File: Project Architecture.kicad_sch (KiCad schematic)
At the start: 0 parts

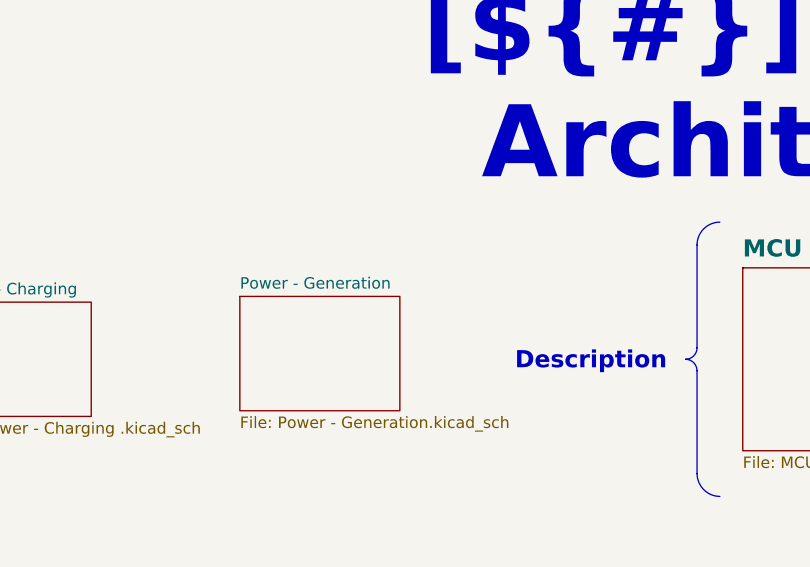
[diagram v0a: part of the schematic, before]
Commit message: added power switch, 5V and 3V3 power generation
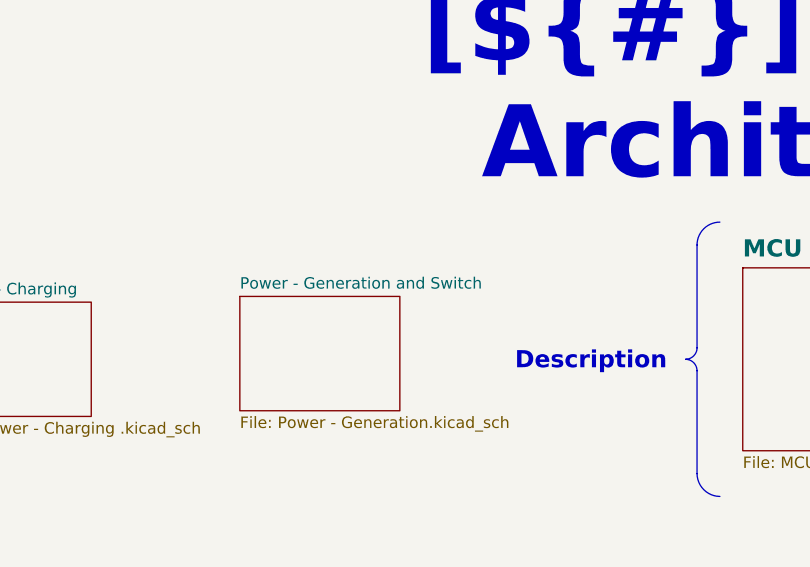
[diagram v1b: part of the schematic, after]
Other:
- sheet Power - Generation renamed Power - Generation and Switch
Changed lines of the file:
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@@
 			(color 0 0 0 0.0000)
 		)
-		(property "Sheetname" "Power - Generation"
+		(property "Sheetname" "Power - Generation and Switch"
 			(at 144.78 49.4534 0)
 			(effects

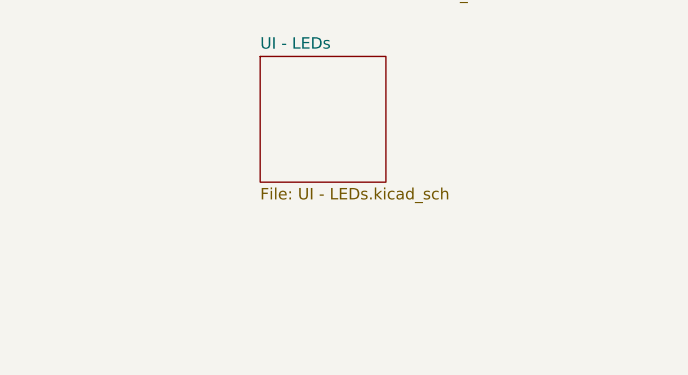
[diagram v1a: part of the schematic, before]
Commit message: added buzzer schematic
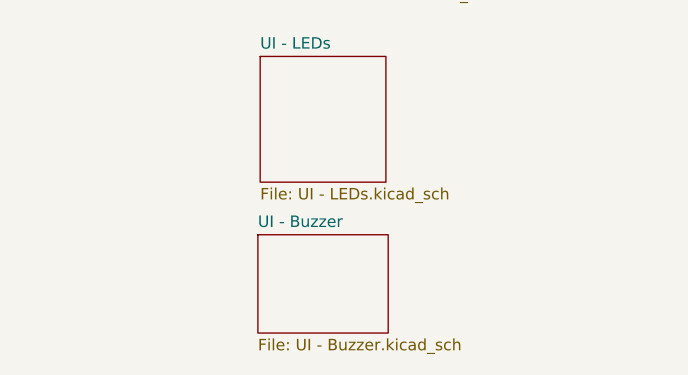
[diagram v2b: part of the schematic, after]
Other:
- added sheet UI - Buzzer (UI - Buzzer.kicad_sch)
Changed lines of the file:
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@@
+	)
+	(sheet
+		(at 282.956 228.092)
+		(size 14.478 10.922)
+		(exclude_from_sim no)
+		(in_bom yes)
+		(on_board yes)
+		(dnp no)
+		(fields_autoplaced yes)
+		(stroke
+			(width 0.1524)
+			(type solid)
+		)
+		(fill
+			(color 0 0 0 0.0000)
+		)
+		(property "Sheetname" "UI - Buzzer"
+			(at 282.956 227.3804 0)
+			(effects
+				(font
+					(size 1.27 1.27)
+				)
+				(justify left bottom)
+			)
+		)
+		(property "Sheetfile" "UI - Buzzer.kicad_sch"
+			(at 282.956 239.5986 0)
+			(effects
+				(font
+					(size 1.27 1.27)
+				)
+				(justify left top)
+			)
+		)
+		(instances
+			(project "transmitter"
+				(path "/0650c7a8-acba-429c-9f8e-eec0baf0bc1c/fede4c36-00cc-4d3d-b71c-5243ba232202"
+					(page "23")
+				)
+			)
+		)
 	)
 	(sheet

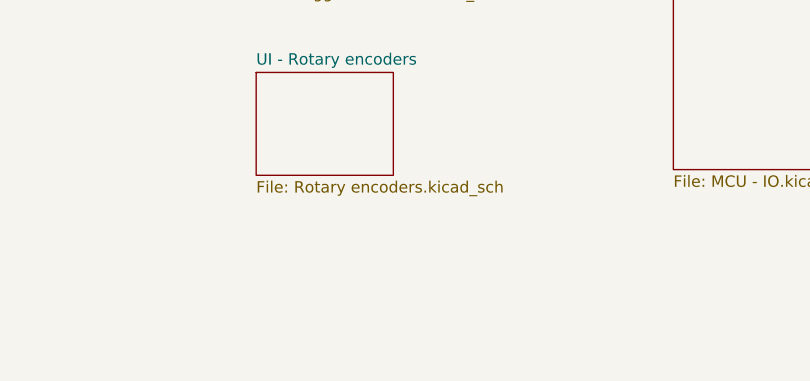
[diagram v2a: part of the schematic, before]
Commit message: added auxiliary schematic, problem with kicad - cannot modify project settings
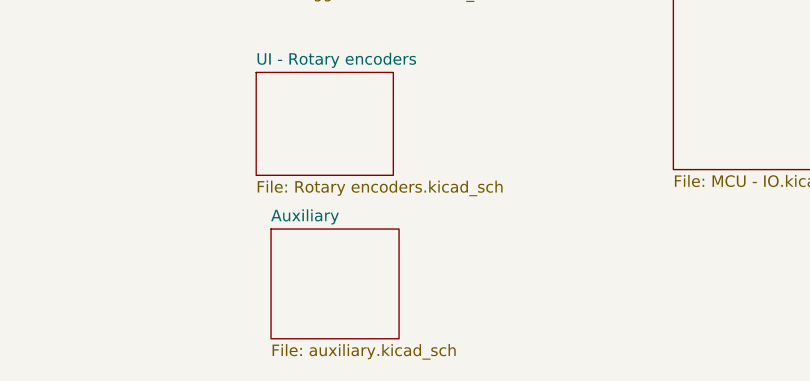
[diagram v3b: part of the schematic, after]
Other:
- added sheet Auxiliary (auxiliary.kicad_sch)
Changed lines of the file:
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@@
+	)
+	(sheet
+		(at 155.956 231.394)
+		(size 14.224 12.192)
+		(exclude_from_sim no)
+		(in_bom yes)
+		(on_board yes)
+		(dnp no)
+		(fields_autoplaced yes)
+		(stroke
+			(width 0.1524)
+			(type solid)
+		)
+		(fill
+			(color 0 0 0 0.0000)
+		)
+		(property "Sheetname" "Auxiliary"
+			(at 155.956 230.6824 0)
+			(effects
+				(font
+					(size 1.27 1.27)
+				)
+				(justify left bottom)
+			)
+		)
+		(property "Sheetfile" "auxiliary.kicad_sch"
+			(at 155.956 244.1706 0)
+			(effects
+				(font
+					(size 1.27 1.27)
+				)
+				(justify left top)
+			)
+		)
+		(instances
+			(project "transmitter"
+				(path "/0650c7a8-acba-429c-9f8e-eec0baf0bc1c/fede4c36-00cc-4d3d-b71c-5243ba232202"
+					(page "24")
+				)
+			)
+		)
 	)
 	(sheet

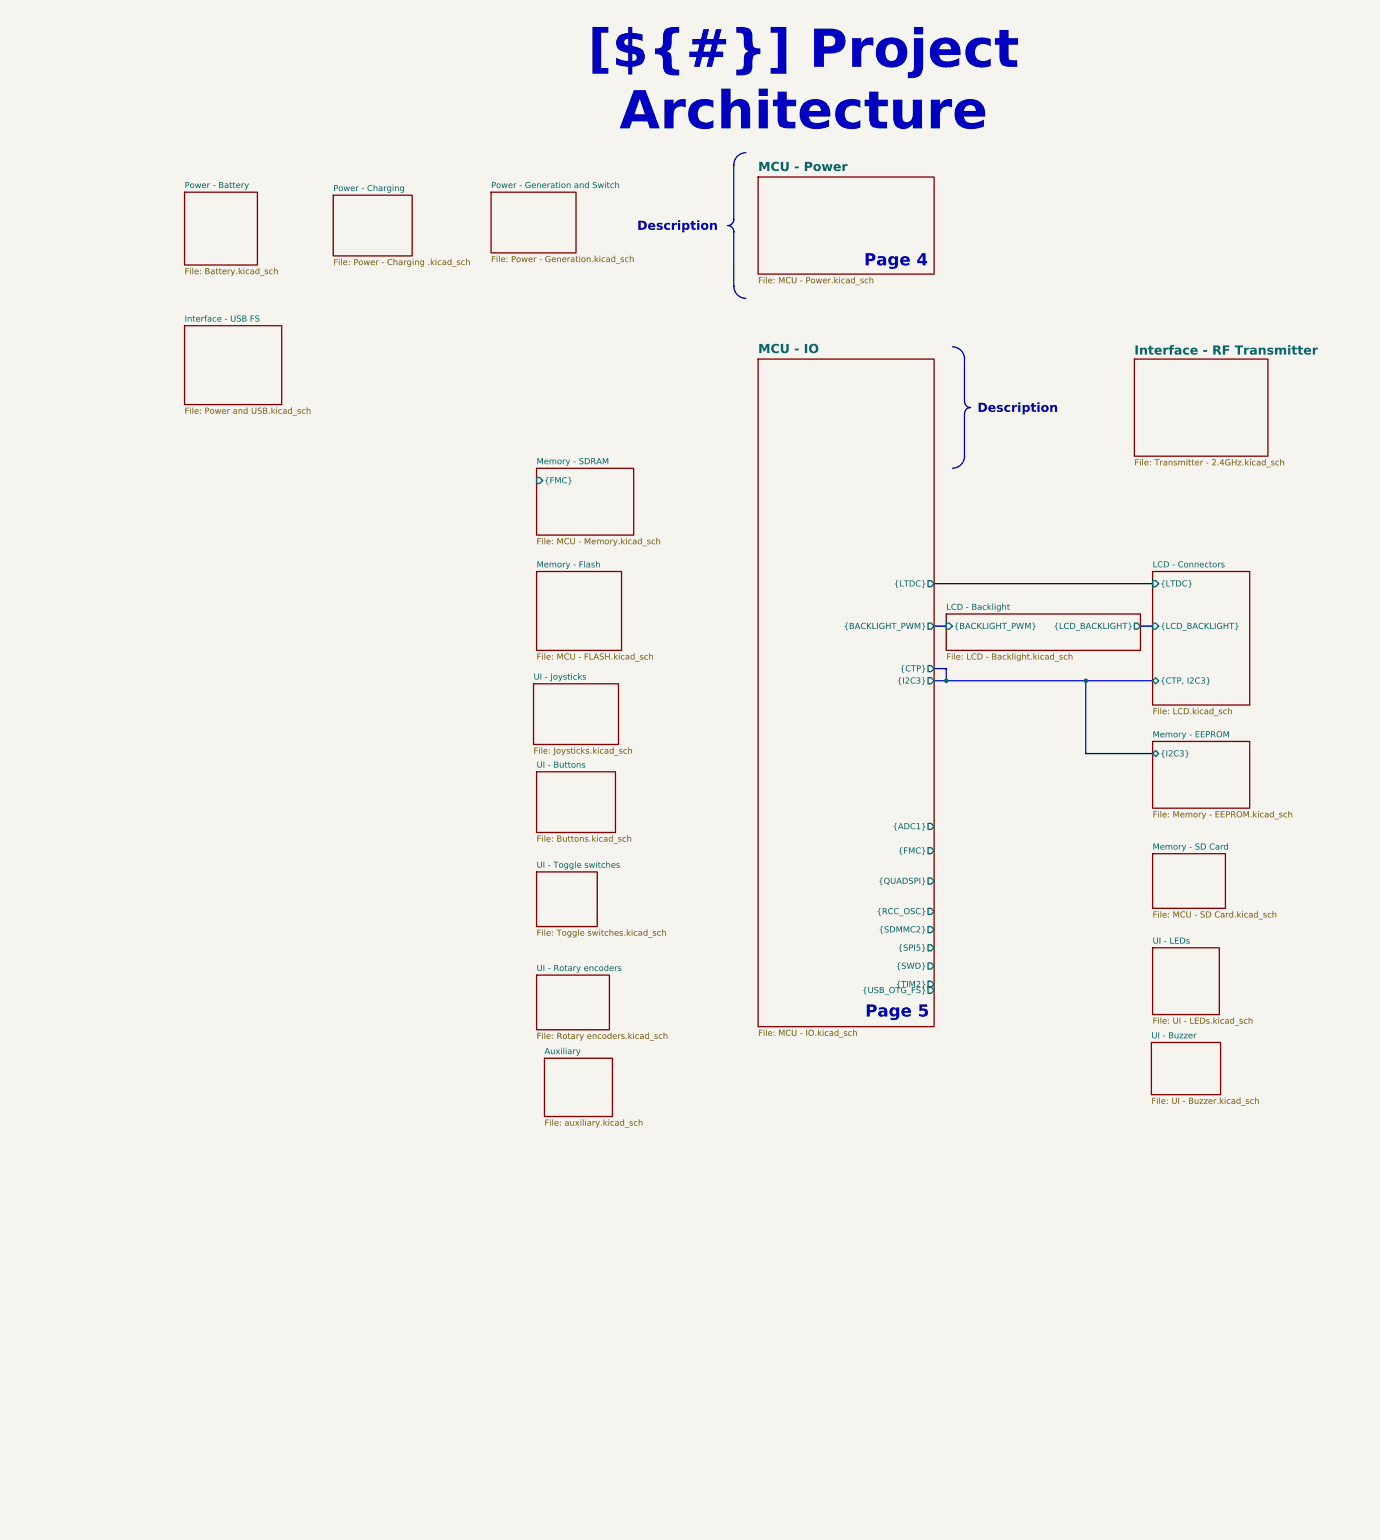
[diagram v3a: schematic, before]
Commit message: update project structure and import to pcb
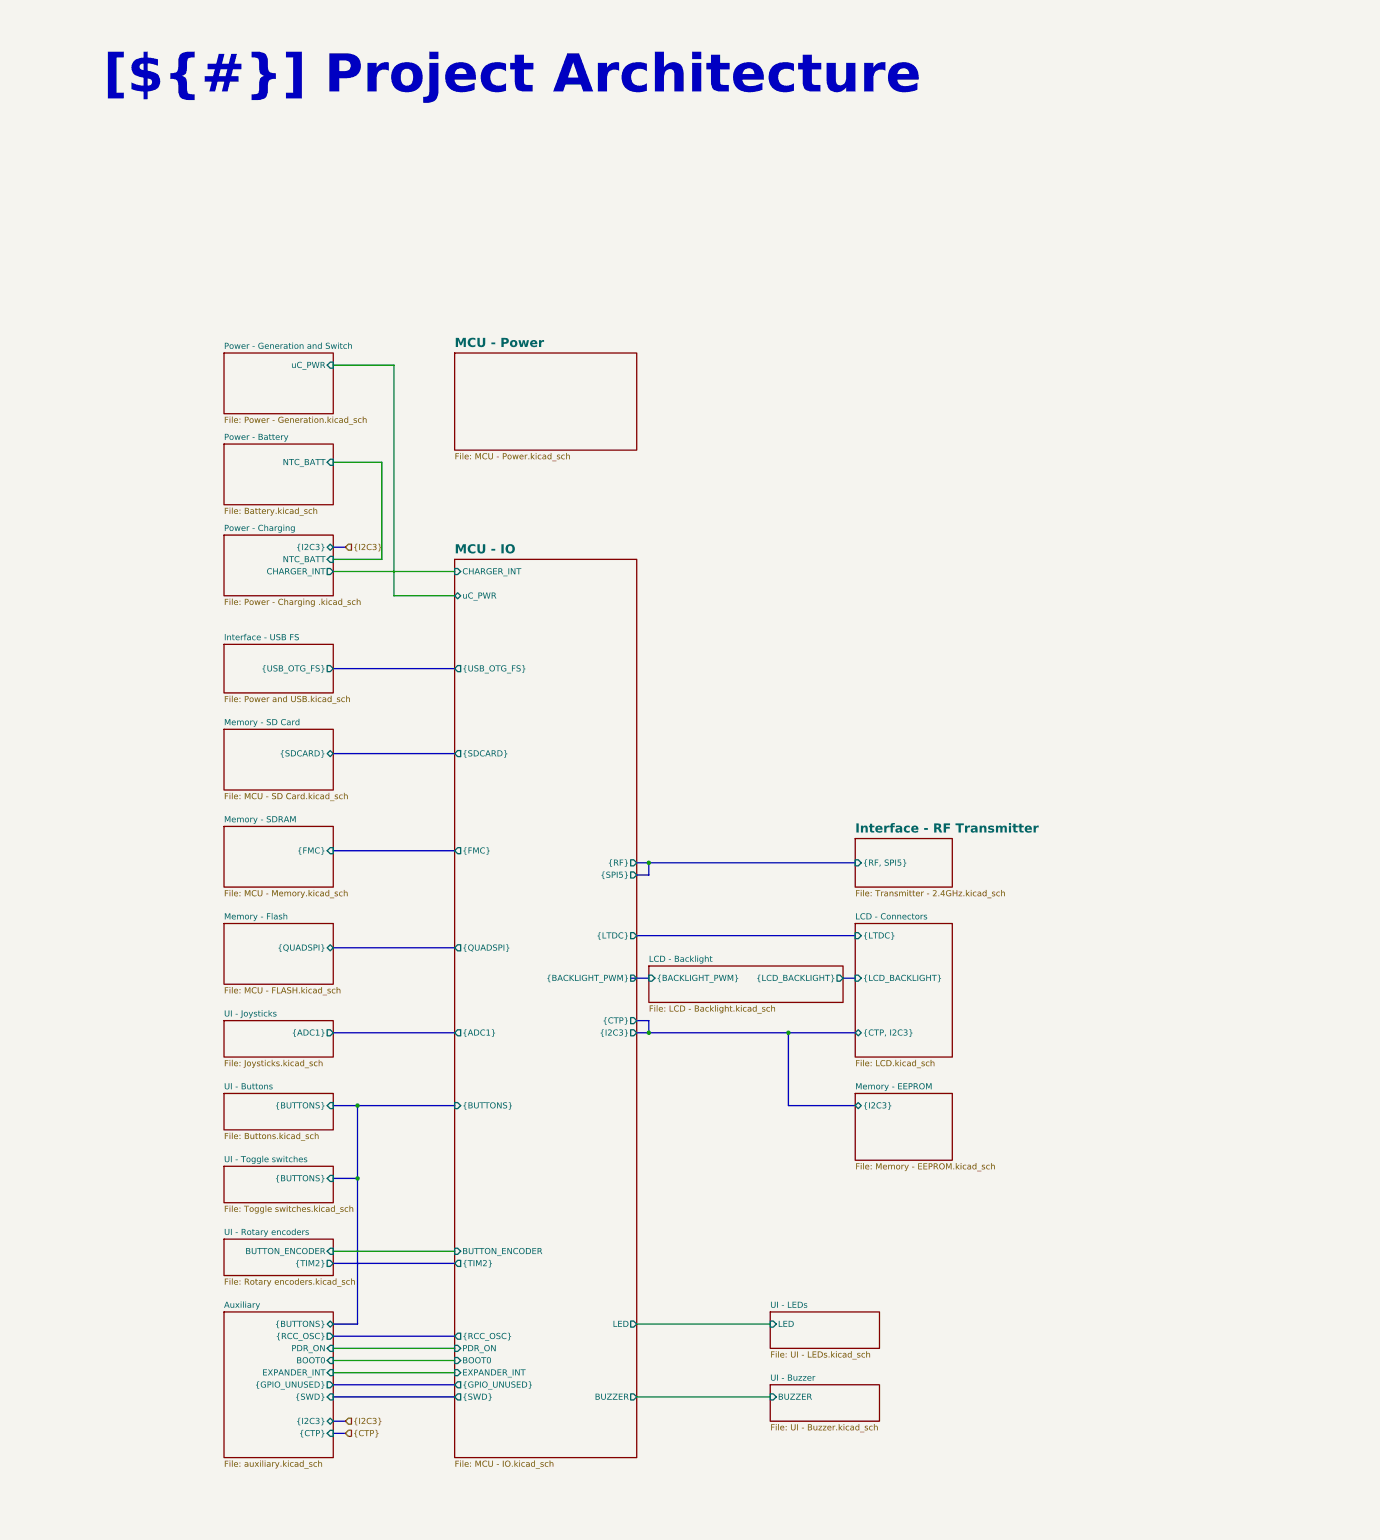
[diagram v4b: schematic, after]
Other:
- sheet Auxiliary ports: added BOOT0, EXPANDER_INT, PDR_ON, {BUTTONS}, {CTP}, {GPIO_UNUSED}, {I2C3}, {RCC_OSC}, {SWD}; removed none
- sheet Interface - RF Transmitter ports: added {RF, SPI5}; removed none
- sheet Interface - USB FS ports: added {USB_OTG_FS}; removed none
- sheet MCU - IO ports: added BOOT0, BUTTON_ENCODER, BUZZER, CHARGER_INT, EXPANDER_INT, LED, PDR_ON, uC_PWR, {BUTTONS}, {GPIO_UNUSED}, {RF}, {SDCARD}; removed {SDMMC2}
- sheet Memory - Flash ports: added {QUADSPI}; removed none
- sheet Memory - SD Card ports: added {SDCARD}; removed none
- sheet Power - Battery ports: added NTC_BATT; removed none
- sheet Power - Charging ports: added CHARGER_INT, NTC_BATT, {I2C3}; removed none
- sheet Power - Generation and Switch ports: added uC_PWR; removed none
- sheet UI - Buttons ports: added {BUTTONS}; removed none
- sheet UI - Buzzer ports: added BUZZER; removed none
- sheet UI - Joysticks ports: added {ADC1}; removed none
- sheet UI - LEDs ports: added LED; removed none
- sheet UI - Rotary encoders ports: added BUTTON_ENCODER, {TIM2}; removed none
- sheet UI - Toggle switches ports: added {BUTTONS}; removed none
- note removed: "Page 4"
- note removed: "Page 5"
